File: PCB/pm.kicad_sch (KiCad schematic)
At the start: 2 parts, among them J2 USB_C_Receptacle_USB2.0_14P, U2 TP4057

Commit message: Made first PCB
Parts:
- added C2, C3: 10uF, Capacitor_SMD:C_0402_1005Metric, symbol Device:C_Small
- added C4: 100n, Capacitor_SMD:C_0402_1005Metric, symbol Device:C_Small
- added D_CHRG, D_STDBY: LED, LED_SMD:LED_0603_1608Metric, symbol Device:LED
- added J3: Conn_01x02_Socket, Connector_PinHeader_2.54mm:PinHeader_1x02_P2.54mm_Horizontal, symbol Connector:Conn_01x02_Socket
- added R1: 2.2k, Resistor_SMD:R_0402_1005Metric, symbol Device:R_Small
- added R2: 5k, Resistor_SMD:R_0402_1005Metric, symbol Device:R_Small
- added R3, R4: 5.1k, Resistor_SMD:R_0402_1005Metric, symbol Device:R_Small
- added R5, R6: 33, Resistor_SMD:R_0402_1005Metric, symbol Device:R_Small
- added R7, R8: 470k, Resistor_SMD:R_0402_1005Metric, symbol Device:R_Small
- added SW1: SW_SPDT, Button_Switch_SMD:SW_SPDT_PCM12, symbol Switch:SW_SPDT
- added U3: AP2127K-3.3, Package_TO_SOT_SMD:SOT-23-5, symbol Regulator_Linear:AP2127K-3.3
- J2: footprint (none) -> Connector_USB:USB_C_Receptacle_G-Switch_GT-USB-7010ASV
- U2: footprint Package_TO_SOT_SMD:TSOT-23-5 -> Package_TO_SOT_SMD:TSOT-23-6
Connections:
- net GND: now also U2.2 (GND), C2.1, C3.2, C4.2, J3.1 (Pin_1), R2.2, R3.1, R4.1, R8.2, U3.2 (GND)
- net VBUS: now reaches J2.A4 (VBUS), J2.A9 (VBUS), J2.B4 (VBUS), J2.B9 (VBUS)
- net VBUS: now also U2.4 (V_{CC}), C3.1, R1.1
- net at J2.A5 (CC1): now also R3.2
- net at J2.A6 (D+): now also J2.B6 (D+), R6.2
- net at J2.A7 (D-): now also J2.B7 (D-), R5.2
- net at J2.B5 (CC2): now also R4.2
- net at U2.1 (~{CHRG}): now also D_CHRG.1 (K)
- net at U2.3 (BAT): now also C2.2, J3.2 (Pin_2), SW1.2 (B)
- net at U2.5 (STDBY): now also D_STDBY.1 (K)
- net at U2.6 (PROG): now also R2.1
- new net: D_CHRG.2 (A), D_STDBY.2 (A), R1.2
- new net: R7.1, SW1.3 (C), U3.1 (VIN), U3.3 (EN)
- new net +3V3: C4.1, U3.5 (VOUT)
- new net BATT_DIV: R7.2, R8.1
- new net USB_DN: R5.1
- new net USB_DP: R6.1
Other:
- moved on the sheet: U2

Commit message: PCB V2
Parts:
- renumbered C2 to C4, C4 to C5, D_CHRG to D_CHRG1, D_STDBY to D_STDBY1, R3 to R1, R4 to R2, R5 to R3, R6 to R4, R1 to R5, R2 to R6, SW1 to SW2
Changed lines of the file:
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@@
 		(on_board yes)
 		(dnp no)
-		(property "Reference" "D_CHRG"
+		(property "Reference" "D_CHRG1"
 			(at 91.44 90.424 0)
 			(effects
@@
 			(project ""
 				(path "/cd633adc-49f5-4b4f-8d72-c74316356641/0a587446-9d59-4f6f-9f4c-a6bc7b3f34e8"
-					(reference "D_CHRG")
+					(reference "D_CHRG1")
 					(unit 1)
 				)
@@
 		(dnp no)
 		(fields_autoplaced yes)
-		(property "Reference" "SW1"
+		(property "Reference" "SW2"
 			(at 167.64 104.14 0)
 			(effects
@@
 			(project ""
 				(path "/cd633adc-49f5-4b4f-8d72-c74316356641/0a587446-9d59-4f6f-9f4c-a6bc7b3f34e8"
-					(reference "SW1")
+					(reference "SW2")
 					(unit 1)
 				)
@@
 		(dnp no)
 		(fields_autoplaced yes)
-		(property "Reference" "#PWR017"
+		(property "Reference" "#PWR012"
 			(at 114.3 118.11 0)
 			(effects
@@
 			(project ""
 				(path "/cd633adc-49f5-4b4f-8d72-c74316356641/0a587446-9d59-4f6f-9f4c-a6bc7b3f34e8"
-					(reference "#PWR017")
+					(reference "#PWR012")
 					(unit 1)
 				)
@@
 		(dnp no)
 		(fields_autoplaced yes)
-		(property "Reference" "C4"
+		(property "Reference" "C5"
 			(at 219.71 116.8462 0)
 			(effects
@@
 			(project ""
 				(path "/cd633adc-49f5-4b4f-8d72-c74316356641/0a587446-9d59-4f6f-9f4c-a6bc7b3f34e8"
-					(reference "C4")
+					(reference "C5")
 					(unit 1)
 				)
@@
 		(dnp no)
 		(fields_autoplaced yes)
-		(property "Reference" "#PWR021"
+		(property "Reference" "#PWR014"
 			(at 217.17 142.24 0)
 			(effects
@@
 			(project ""
 				(path "/cd633adc-49f5-4b4f-8d72-c74316356641/0a587446-9d59-4f6f-9f4c-a6bc7b3f34e8"
-					(reference "#PWR021")
+					(reference "#PWR014")
 					(unit 1)
 				)
@@
 		(dnp no)
 		(fields_autoplaced yes)
-		(property "Reference" "#PWR019"
+		(property "Reference" "#PWR011"
 			(at 64.77 91.44 0)
 			(effects
@@
 			(project ""
 				(path "/cd633adc-49f5-4b4f-8d72-c74316356641/0a587446-9d59-4f6f-9f4c-a6bc7b3f34e8"
-					(reference "#PWR019")
+					(reference "#PWR011")
 					(unit 1)
 				)
@@
 		(on_board yes)
 		(dnp no)
-		(property "Reference" "R5"
+		(property "Reference" "R3"
 			(at 53.34 102.362 90)
 			(effects
@@
 			(project "sponka"
 				(path "/cd633adc-49f5-4b4f-8d72-c74316356641/0a587446-9d59-4f6f-9f4c-a6bc7b3f34e8"
-					(reference "R5")
+					(reference "R3")
 					(unit 1)
 				)
@@
 		(dnp no)
 		(fields_autoplaced yes)
-		(property "Reference" "R1"
+		(property "Reference" "R5"
 			(at 86.36 92.71 90)
 			(effects
@@
 			(project ""
 				(path "/cd633adc-49f5-4b4f-8d72-c74316356641/0a587446-9d59-4f6f-9f4c-a6bc7b3f34e8"
-					(reference "R1")
+					(reference "R5")
 					(unit 1)
 				)
@@
 		(dnp no)
 		(fields_autoplaced yes)
-		(property "Reference" "R2"
+		(property "Reference" "R6"
 			(at 127 105.4099 0)
 			(effects
@@
 			(project ""
 				(path "/cd633adc-49f5-4b4f-8d72-c74316356641/0a587446-9d59-4f6f-9f4c-a6bc7b3f34e8"
-					(reference "R2")
+					(reference "R6")
 					(unit 1)
 				)
@@
 		(dnp no)
 		(fields_autoplaced yes)
-		(property "Reference" "#PWR018"
+		(property "Reference" "#PWR013"
 			(at 156.21 85.09 0)
 			(effects
@@
 			(project ""
 				(path "/cd633adc-49f5-4b4f-8d72-c74316356641/0a587446-9d59-4f6f-9f4c-a6bc7b3f34e8"
-					(reference "#PWR018")
+					(reference "#PWR013")
 					(unit 1)
 				)
@@
 		(dnp no)
 		(fields_autoplaced yes)
-		(property "Reference" "C2"
+		(property "Reference" "C4"
 			(at 134.62 91.4462 0)
 			(effects
@@
 			(project ""
 				(path "/cd633adc-49f5-4b4f-8d72-c74316356641/0a587446-9d59-4f6f-9f4c-a6bc7b3f34e8"
-					(reference "C2")
+					(reference "C4")
 					(unit 1)
 				)
@@
 		(on_board yes)
 		(dnp no)
-		(property "Reference" "R4"
+		(property "Reference" "R2"
 			(at 53.34 95.758 90)
 			(effects
@@
 			(project "sponka"
 				(path "/cd633adc-49f5-4b4f-8d72-c74316356641/0a587446-9d59-4f6f-9f4c-a6bc7b3f34e8"
-					(reference "R4")
+					(reference "R2")
 					(unit 1)
 				)
@@
 		(on_board yes)
 		(dnp no)
-		(property "Reference" "R3"
+		(property "Reference" "R1"
 			(at 53.34 86.106 90)
 			(effects
@@
 			(project ""
 				(path "/cd633adc-49f5-4b4f-8d72-c74316356641/0a587446-9d59-4f6f-9f4c-a6bc7b3f34e8"
-					(reference "R3")
+					(reference "R1")
 					(unit 1)
 				)
@@
 		(dnp no)
 		(fields_autoplaced yes)
-		(property "Reference" "#PWR016"
+		(property "Reference" "#PWR010"
 			(at 35.56 134.62 0)
 			(effects
@@
 			(project ""
 				(path "/cd633adc-49f5-4b4f-8d72-c74316356641/0a587446-9d59-4f6f-9f4c-a6bc7b3f34e8"
-					(reference "#PWR016")
+					(reference "#PWR010")
 					(unit 1)
 				)
@@
 		(on_board yes)
 		(dnp no)
-		(property "Reference" "R6"
+		(property "Reference" "R4"
 			(at 53.34 107.442 90)
 			(effects
@@
 			(project "sponka"
 				(path "/cd633adc-49f5-4b4f-8d72-c74316356641/0a587446-9d59-4f6f-9f4c-a6bc7b3f34e8"
-					(reference "R6")
+					(reference "R4")
 					(unit 1)
 				)
@@
 		(on_board yes)
 		(dnp no)
-		(property "Reference" "D_STDBY"
+		(property "Reference" "D_STDBY1"
 			(at 91.186 103.632 0)
 			(effects
@@
 			(project "sponka"
 				(path "/cd633adc-49f5-4b4f-8d72-c74316356641/0a587446-9d59-4f6f-9f4c-a6bc7b3f34e8"
-					(reference "D_STDBY")
-					(unit 1)
-				)
+					(reference "D_STDBY1")
+					(unit 1)
+				)

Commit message: New PCB revision
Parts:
- J3: footprint Connector_PinHeader_2.54mm:PinHeader_1x02_P2.54mm_Horizontal -> sponka:HDR-SMD_2P-P2.54-H-M-W13.3-N
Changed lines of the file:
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@@
 			)
 		)
-		(property "Footprint" "Connector_PinHeader_2.54mm:PinHeader_1x02_P2.54mm_Horizontal"
+		(property "Footprint" "sponka:HDR-SMD_2P-P2.54-H-M-W13.3-N"
 			(at 161.29 92.71 0)
 			(effects

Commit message: Progress update
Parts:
- removed D_STDBY1: LED, LED_SMD:LED_0603_1608Metric, symbol Device:LED
- J3: footprint sponka:HDR-SMD_2P-P2.54-H-M-W13.3-N -> Connector_JST:JST_PH_B2B-PH-SM4-TB_1x02-1MP_P2.00mm_Vertical
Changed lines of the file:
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@@
-	)
-	(junction
-		(at 92.71 97.79)
-		(diameter 0)
-		(color 0 0 0 0)
 	)
 	(junction
@@
 	(wire
 		(pts
-			(xy 100.33 100.33) (xy 104.14 100.33)
-		)
-		(stroke
-			(width 0)
-			(type default)
-		)
-	)
-	(wire
-		(pts
 			(xy 100.33 95.25) (xy 104.14 95.25)
 		)
@@
 		(pts
 			(xy 228.6 120.65) (xy 217.17 120.65)
-		)
-		(stroke
-			(width 0)
-			(type default)
-		)
-	)
-	(wire
-		(pts
-			(xy 92.71 97.79) (xy 92.71 100.33)
 		)
 		(stroke
@@
 			)
 		)
-		(property "Footprint" "sponka:HDR-SMD_2P-P2.54-H-M-W13.3-N"
+		(property "Footprint" "Connector_JST:JST_PH_B2B-PH-SM4-TB_1x02-1MP_P2.00mm_Vertical"
 			(at 161.29 92.71 0)
 			(effects
@@
 					(unit 1)
 				)
-			)
-		)
-	)
-	(symbol
-		(lib_id "Device:LED")
-		(at 96.52 100.33 180)
-		(unit 1)
-		(exclude_from_sim no)
-		(in_bom yes)
-		(on_board yes)
-		(dnp no)
-		(property "Reference" "D_STDBY1"
-			(at 91.186 103.632 0)
-			(effects
-				(font
-					(size 1.27 1.27)
-				)
-				(justify right)
-			)
-		)
-		(property "Value" "LED"
-			(at 91.186 105.664 0)
-			(effects
-				(font
-					(size 1.27 1.27)
-				)
-				(justify right)
-			)
-		)
-		(property "Footprint" "LED_SMD:LED_0603_1608Metric"
-			(at 96.52 100.33 0)
-			(effects
-				(font
-					(size 1.27 1.27)
-				)
-				(hide yes)
-			)
-		)
-		(property "Datasheet" "~"
-			(at 96.52 100.33 0)
-			(effects
-				(font
-					(size 1.27 1.27)
-				)
-				(hide yes)
-			)
-		)
-		(property "Description" "Light emitting diode"
-			(at 96.52 100.33 0)
-			(effects
-				(font
-					(size 1.27 1.27)
-				)
-				(hide yes)
-			)
-		)
-		(pin "2"
-		)
-		(pin "1"
-		)
-		(instances
-			(project "sponka"
-				(path "/cd633adc-49f5-4b4f-8d72-c74316356641/0a587446-9d59-4f6f-9f4c-a6bc7b3f34e8"
-					(reference "D_STDBY1")
-					(unit 1)
-				)

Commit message: Ma favorite design yet!
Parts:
- J3: footprint Connector_JST:JST_PH_B2B-PH-SM4-TB_1x02-1MP_P2.00mm_Vertical -> Connector_JST:JST_ACH_BM02B-ACHSS-GAN-ETF_1x02-1MP_P1.20mm_Vertical
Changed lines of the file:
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@@
 			)
 		)
-		(property "Footprint" "Connector_JST:JST_PH_B2B-PH-SM4-TB_1x02-1MP_P2.00mm_Vertical"
+		(property "Footprint" "Connector_JST:JST_ACH_BM02B-ACHSS-GAN-ETF_1x02-1MP_P1.20mm_Vertical"
 			(at 161.29 92.71 0)
 			(effects

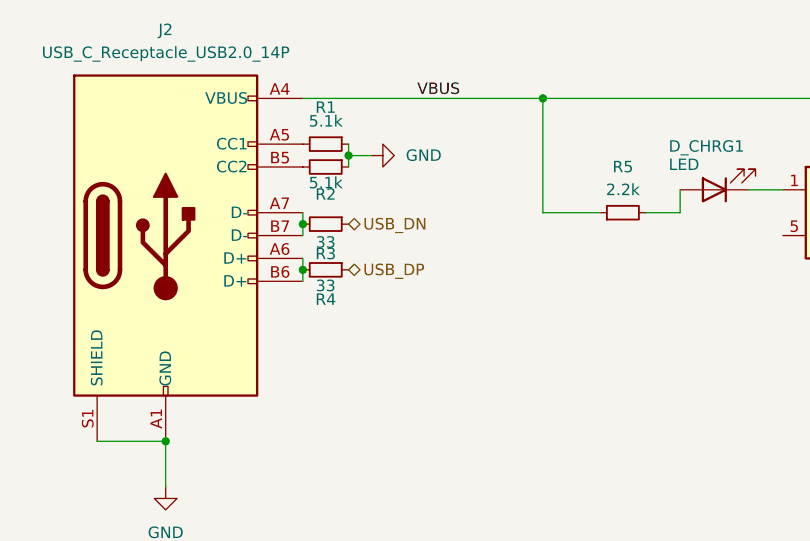
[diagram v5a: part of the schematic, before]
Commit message: Update the backside
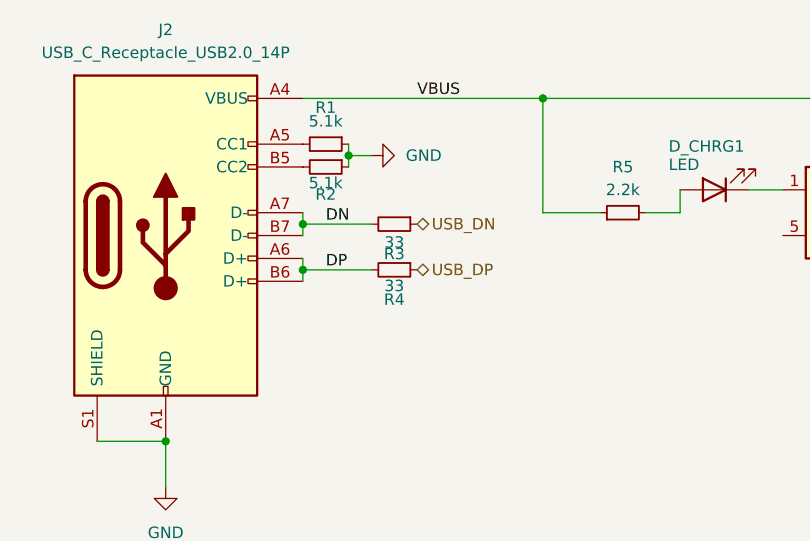
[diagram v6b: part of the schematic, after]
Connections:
- net DP: now reaches J2.A6 (D+), J2.B6 (D+), R4.2
- net DN: now reaches J2.A7 (D-), J2.B7 (D-), R3.2
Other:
- moved on the sheet: R3, R4
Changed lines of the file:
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@@
+	(wire
+		(pts
+			(xy 58.42 104.14) (xy 50.8 104.14)
+		)
+		(stroke
+			(width 0)
+			(type default)
+		)
+	)
 	(wire
 		(pts
@@
 	(wire
 		(pts
+			(xy 58.42 99.06) (xy 50.8 99.06)
+		)
+		(stroke
+			(width 0)
+			(type default)
+		)
+	)
+	(wire
+		(pts
 			(xy 77.47 97.79) (xy 77.47 85.09)
 		)
@@
 		)
 	)
-	(label "VBUS"
-		(at 63.5 85.09 0)
+	(label "DP"
+		(at 53.34 104.14 0)
 		(fields_autoplaced yes)
 		(effects
@@
 		)
 	)
-	(hierarchical_label "USB_DP"
-		(shape bidirectional)
-		(at 55.88 104.14 0)
+	(label "DN"
+		(at 53.34 99.06 0)
 		(fields_autoplaced yes)
 		(effects
@@
 				(size 1.27 1.27)
 			)
+			(justify left bottom)
+		)
+	)
+	(label "VBUS"
+		(at 63.5 85.09 0)
+		(fields_autoplaced yes)
+		(effects
+			(font
+				(size 1.27 1.27)
+			)
+			(justify left bottom)
+		)
+	)
+	(hierarchical_label "USB_DP"
+		(shape bidirectional)
+		(at 63.5 104.14 0)
+		(fields_autoplaced yes)
+		(effects
+			(font
+				(size 1.27 1.27)
+			)
 			(justify left)
 		)
@@
 	(hierarchical_label "USB_DN"
 		(shape bidirectional)
-		(at 55.88 99.06 0)
+		(at 63.5 99.06 0)
 		(fields_autoplaced yes)
 		(effects
@@
 	(symbol
 		(lib_id "Device:R_Small")
-		(at 53.34 99.06 270)
+		(at 60.96 99.06 270)
 		(unit 1)
 		(exclude_from_sim no)
@@
 		(dnp no)
 		(property "Reference" "R3"
-			(at 53.34 102.362 90)
+			(at 60.96 102.362 90)
 			(effects
 				(font
@@
 		)
 		(property "Value" "33"
-			(at 53.34 101.092 90)
+			(at 60.96 101.092 90)
 			(effects
 				(font
@@
 		)
 		(property "Footprint" "Resistor_SMD:R_0402_1005Metric"
-			(at 53.34 99.06 0)
+			(at 60.96 99.06 0)
 			(effects
 				(font
@@
 		)
 		(property "Datasheet" "~"
-			(at 53.34 99.06 0)
+			(at 60.96 99.06 0)
 			(effects
 				(font
@@
 		)
 		(property "Description" "Resistor, small symbol"
-			(at 53.34 99.06 0)
+			(at 60.96 99.06 0)
 			(effects
 				(font
@@
 	(symbol
 		(lib_id "Device:R_Small")
-		(at 53.34 104.14 270)
+		(at 60.96 104.14 270)
 		(unit 1)
 		(exclude_from_sim no)
@@
 		(dnp no)
 		(property "Reference" "R4"
-			(at 53.34 107.442 90)
+			(at 60.96 107.442 90)
 			(effects
 				(font
@@
 		)
 		(property "Value" "33"
-			(at 53.34 105.918 90)
+			(at 60.96 105.918 90)
 			(effects
 				(font
@@
 		)
 		(property "Footprint" "Resistor_SMD:R_0402_1005Metric"
-			(at 53.34 104.14 0)
+			(at 60.96 104.14 0)
 			(effects
 				(font
@@
 		)
 		(property "Datasheet" "~"
-			(at 53.34 104.14 0)
+			(at 60.96 104.14 0)
 			(effects
 				(font
@@
 		)
 		(property "Description" "Resistor, small symbol"
-			(at 53.34 104.14 0)
-			(effects
-				(font
+			(at 60.96 104.14 0)
+			(effects
+				(font

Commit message: Change the battery connector resolve issues
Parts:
- J3: footprint Connector_JST:JST_ACH_BM02B-ACHSS-GAN-ETF_1x02-1MP_P1.20mm_Vertical -> Connector_JST:JST_SH_SM02B-SRSS-TB_1x02-1MP_P1.00mm_Horizontal
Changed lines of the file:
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@@
 			)
 		)
-		(property "Footprint" "Connector_JST:JST_ACH_BM02B-ACHSS-GAN-ETF_1x02-1MP_P1.20mm_Vertical"
+		(property "Footprint" "Connector_JST:JST_SH_SM02B-SRSS-TB_1x02-1MP_P1.00mm_Horizontal"
 			(at 161.29 92.71 0)
 			(effects

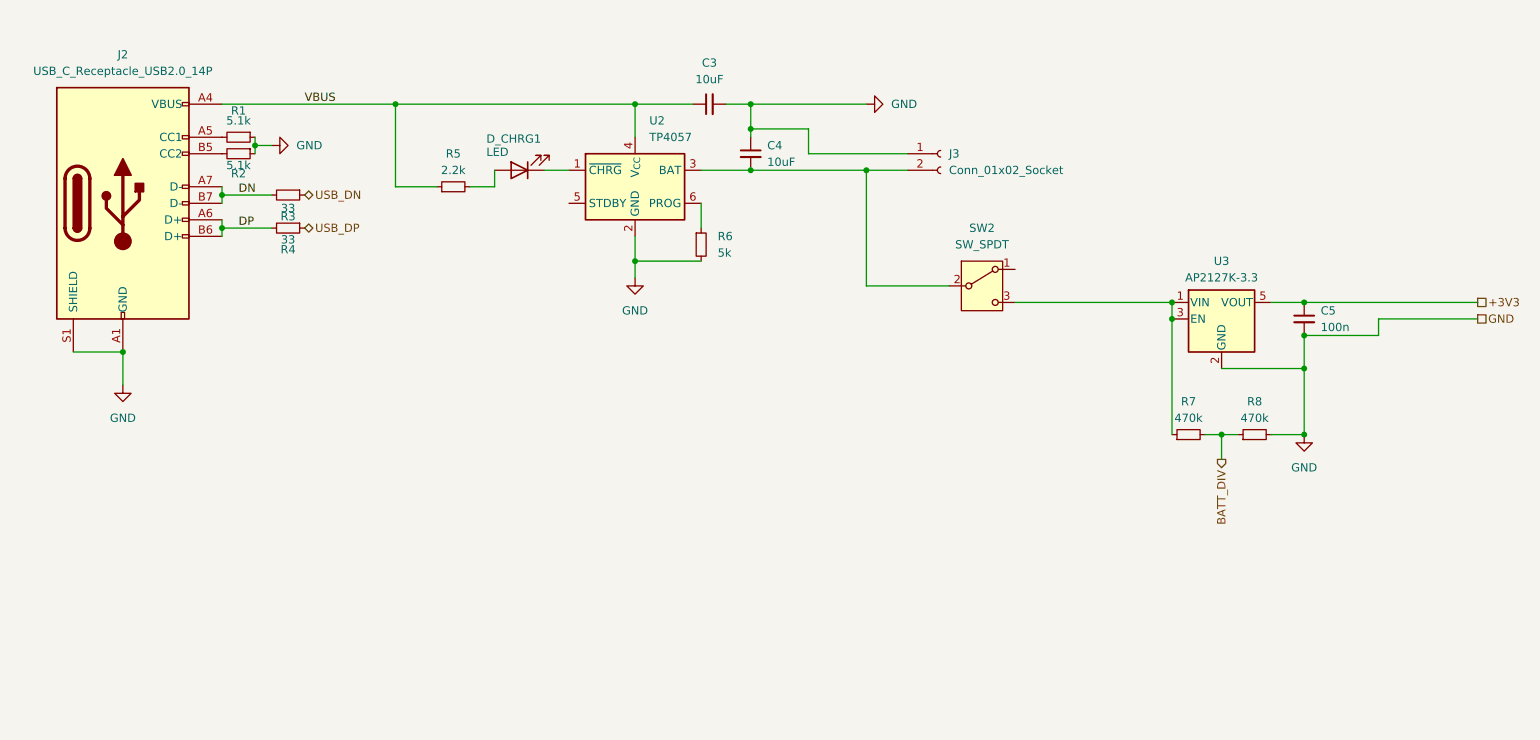
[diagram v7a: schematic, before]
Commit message: Add battery protection circuit
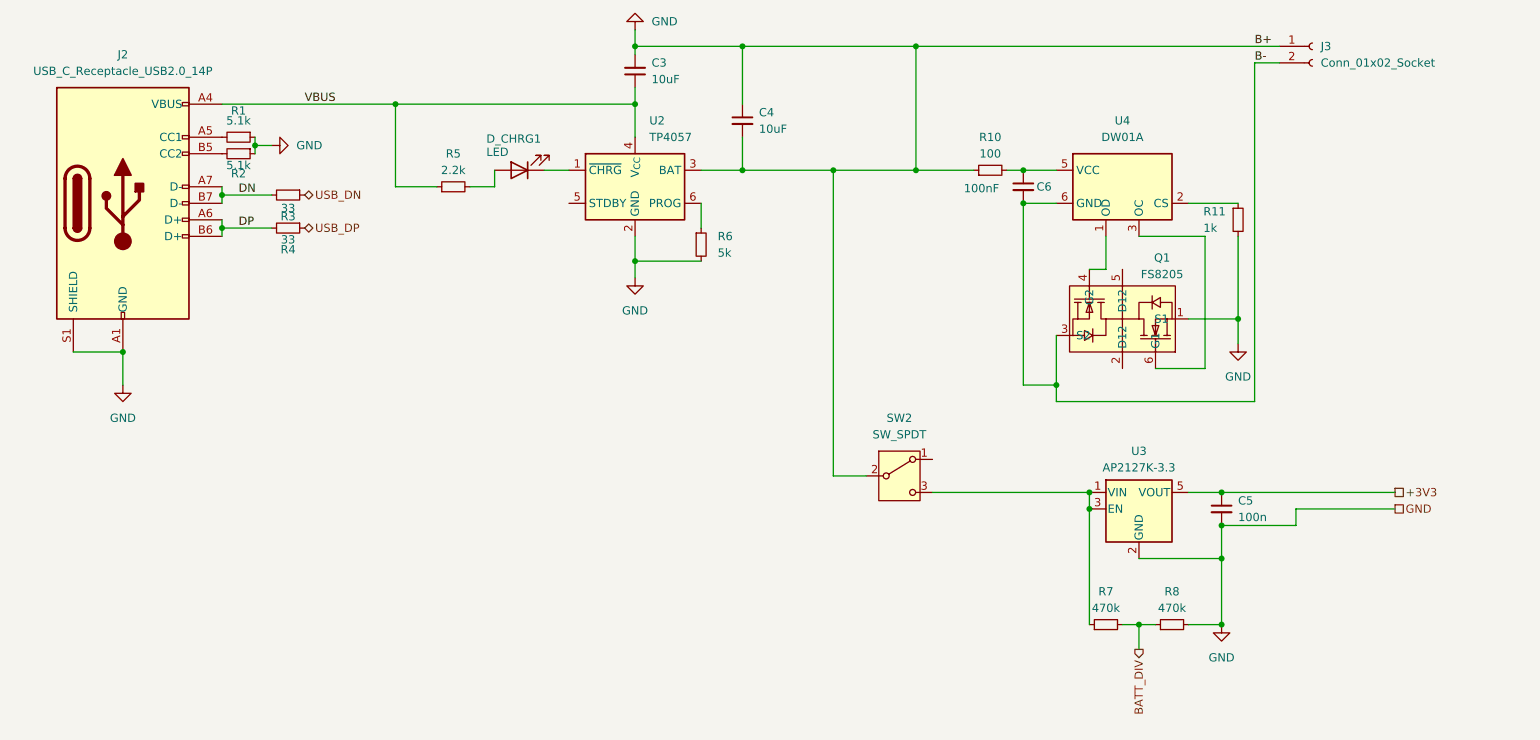
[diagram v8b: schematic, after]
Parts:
- added C6: 100nF, symbol Device:C_Small
- added Q1: FS8205, easyeda2kicad:SOT-23-6_L2.9-W1.6-P0.95-LS2.8-BR, symbol easyeda2kicad:FS8205
- added R10: 100, symbol Device:R_Small
- added R11: 1k, symbol Device:R_Small
- added U4: DW01A, Package_TO_SOT_SMD:SOT-23-6, symbol Battery_Management:DW01A
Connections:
- net GND: now also C4.2, SW2.2 (B), U2.3 (BAT), Q1.1 (S1), R10.1, R11.2
- new net: R11.1, U4.2 (CS)
- new net: Q1.4 (G2), U4.1 (OD)
- new net: Q1.6 (G1), U4.3 (OC)
- new net: C6.1, R10.2, U4.5 (VCC)
- new net B-: C6.2, J3.2 (Pin_2), Q1.3 (S2), U4.6 (GND)
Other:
- moved on the sheet: C3, C4, C5, J3, R7, R8, SW2, U3
